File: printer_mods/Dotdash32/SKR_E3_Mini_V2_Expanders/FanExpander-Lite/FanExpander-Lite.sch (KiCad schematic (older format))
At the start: 31 parts, among them J1 FAN1_IN, J10 FAN2, J11 V_SELECT3, J12 V_SELECT4, J13 FAN3, J14 FAN4, J2 IO_PassThrough, J3 EXP1_IN, J6 V_SELECT1, J7 V_SELECT2, J9 FAN1, Q1 IRLML6344, Q2 IRLML6344, Q3 IRLML6344

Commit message: feat: init routing of Lite board
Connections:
- net FAN2: now also J3.8 (Pin_8); no longer J3.1 (Pin_1)
- net FAN3: now also J3.6 (Pin_6); no longer J3.3 (Pin_3)
- net FAN4: now also J3.2 (Pin_2); no longer J3.5 (Pin_5)
- net PASS0: now also J3.1 (Pin_1); no longer J3.7 (Pin_7)
- net PASS1: now also J3.3 (Pin_3); no longer J3.2 (Pin_2)
- net PASS2: now also J3.5 (Pin_5); no longer J3.6 (Pin_6)
- net PASS3: now also J3.7 (Pin_7); no longer J3.8 (Pin_8)
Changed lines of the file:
@@
 encoding utf-8
 Sheet 1 1
-Title "SKR E3 Mini Fan Expander"
-Date "2021-12-17"
-Rev "V0.1.0"
+Title "SKR E3 Mini Fan Expander Lite"
+Date "2021-12-18"
+Rev "V0.1.1"
 Comp "Voron Design"
 Comment1 "Drawn by Dotdash32 (JDeW)"
@@
 Wire Wire Line
 	550  1450 850  1450
-Text Label 550  1450 0    50   ~ 0
+Text Label 1650 1750 2    50   ~ 0
 FAN2
 Wire Wire Line
@@
 Wire Wire Line
 	850  1650 550  1650
-Text Label 550  1550 0    50   ~ 0
+Text Label 1650 1650 2    50   ~ 0
 FAN3
-Text Label 550  1650 0    50   ~ 0
+Text Label 1650 1450 2    50   ~ 0
 FAN4
 $Comp
@@
 Wire Wire Line
 	1350 1750 1650 1750
+Text Label 550  1450 0    50   ~ 0
+PASS0
+Text Label 550  1550 0    50   ~ 0
+PASS1
+Text Label 550  1650 0    50   ~ 0
+PASS2
 Text Label 550  1750 0    50   ~ 0
-PASS0
-Text Label 1650 1450 2    50   ~ 0
-PASS1
-Text Label 1650 1650 2    50   ~ 0
-PASS2
-Text Label 1650 1750 2    50   ~ 0
 PASS3
 Text Notes 2100 700  0    100  ~ 0

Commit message: chore: cleanup edges, silkscreen, making pretty
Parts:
- F1: value Polyfuse-2A -> Polyfuse-3A
- renumbered D3 to D1, D4 to D2, D5 to D3, D6 to D4, F3 to F2, J9 to J1, J10 to J2, J13 to J3, J14 to J4, J3 to J5, J1 to J6, J2 to J7, J6 to JP1, J7 to JP2, J11 to JP3, J12 to JP4, JP2 to JP5, R2 to R1, R3 to R2, R6 to R3, R5 to R4, R7 to R5, R11 to R6, R9 to R7, R12 to R9
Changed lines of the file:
@@
 $EndComp
 $Comp
-L Connector_Generic:Conn_01x02 J1
+L Connector_Generic:Conn_01x02 J6
 U 1 1 61C0DEDC
 P 800 3400
-F 0 "J1" H 718 3075 50  0000 C CNN
+F 0 "J6" H 718 3075 50  0000 C CNN
 F 1 "FAN1_IN" H 718 3166 50  0000 C CNN
 F 2 "Connectors_JST:JST_XH_B02B-XH-A_02x2.50mm_Straight" H 800 3400 50  0001 C CNN
@@
 P 2900 900
 F 0 "F1" V 3100 850 50  0000 L CNN
-F 1 "Polyfuse-2A" V 3000 650 50  0000 L CNN
+F 1 "Polyfuse-3A" V 3000 650 50  0000 L CNN
 F 2 "Fuse_Holders_and_Fuses:Fuse_SMD1206_HandSoldering" H 2950 700 50  0001 L CNN
 F 3 "~" H 2900 900 50  0001 C CNN
@@
 	500  3550 2000 3550
 $Comp
-L Connector_Generic:Conn_01x02 J9
+L Connector_Generic:Conn_01x02 J1
 U 1 1 61C7EF42
 P 7350 1400
-F 0 "J9" H 7430 1392 50  0000 L CNN
+F 0 "J1" H 7430 1392 50  0000 L CNN
 F 1 "FAN1" H 7430 1301 50  0000 L CNN
 F 2 "Connectors_JST:JST_XH_B02B-XH-A_02x2.50mm_Straight" H 7350 1400 50  0001 C CNN
@@
 $EndComp
 $Comp
-L Jumper:Jumper_3_Open J6
+L Jumper:Jumper_3_Open JP1
 U 1 1 61C814B1
 P 6800 1250
-F 0 "J6" H 6850 1450 50  0000 R CNN
+F 0 "JP1" H 6850 1450 50  0000 R CNN
 F 1 "V_SELECT1" H 7000 1350 50  0000 R CNN
 F 2 "Pin_Headers:Pin_Header_Straight_1x03_Pitch2.54mm" H 6800 1250 50  0001 C CNN
@@
 FAN1_Drive
 $Comp
-L Device:R_US R2
+L Device:R_US R1
 U 1 1 61C92F81
 P 6100 1500
-F 0 "R2" V 6305 1500 50  0000 C CNN
+F 0 "R1" V 6305 1500 50  0000 C CNN
 F 1 "560R" V 6214 1500 50  0000 C CNN
 F 2 "Resistors_SMD:R_0603_HandSoldering" V 6140 1490 50  0001 C CNN
@@
 $EndComp
 $Comp
-L Connector_Generic:Conn_01x02 J10
+L Connector_Generic:Conn_01x02 J2
 U 1 1 61CF5CB7
 P 9900 1400
-F 0 "J10" H 9980 1392 50  0000 L CNN
+F 0 "J2" H 9980 1392 50  0000 L CNN
 F 1 "FAN2" H 9980 1301 50  0000 L CNN
 F 2 "Connectors_JST:JST_XH_B02B-XH-A_02x2.50mm_Straight" H 9900 1400 50  0001 C CNN
@@
 $EndComp
 $Comp
-L Jumper:Jumper_3_Open J7
+L Jumper:Jumper_3_Open JP2
 U 1 1 61CF5CBD
 P 9350 1250
-F 0 "J7" H 9400 1450 50  0000 R CNN
+F 0 "JP2" H 9400 1450 50  0000 R CNN
 F 1 "V_SELECT2" H 9550 1350 50  0000 R CNN
 F 2 "Pin_Headers:Pin_Header_Straight_1x03_Pitch2.54mm" H 9350 1250 50  0001 C CNN
@@
 $EndComp
 $Comp
-L Device:R_US R3
+L Device:R_US R2
 U 1 1 61CF5CD5
 P 8700 1450
-F 0 "R3" V 8905 1450 50  0000 C CNN
+F 0 "R2" V 8905 1450 50  0000 C CNN
 F 1 "560R" V 8814 1450 50  0000 C CNN
 F 2 "Resistors_SMD:R_0603_HandSoldering" V 8740 1440 50  0001 C CNN
@@
 $EndComp
 $Comp
-L Device:LED D4
+L Device:LED D2
 U 1 1 61CF5CDB
 P 8900 1600
-F 0 "D4" V 8939 1483 50  0000 R CNN
+F 0 "D2" V 8939 1483 50  0000 R CNN
 F 1 "LED" V 8848 1483 50  0000 R CNN
 F 2 "LEDs:LED_0603_HandSoldering" H 8900 1600 50  0001 C CNN
@@
 Connection ~ 9550 1600
 $Comp
-L Device:R_US R6
+L Device:R_US R3
 U 1 1 61D23E6E
 P 9000 1950
-F 0 "R6" V 8795 1950 50  0000 C CNN
+F 0 "R3" V 8795 1950 50  0000 C CNN
 F 1 "100R" V 8886 1950 50  0000 C CNN
 F 2 "Resistors_SMD:R_0603_HandSoldering" V 9040 1940 50  0001 C CNN
@@
 	9550 1600 9550 1750
 $Comp
-L Device:LED D3
+L Device:LED D1
 U 1 1 61C95144
 P 6350 1650
-F 0 "D3" V 6389 1533 50  0000 R CNN
+F 0 "D1" V 6389 1533 50  0000 R CNN
 F 1 "LED" V 6298 1533 50  0000 R CNN
 F 2 "LEDs:LED_0603_HandSoldering" H 6350 1650 50  0001 C CNN
@@
 $EndComp
 $Comp
-L Connector_Generic:Conn_01x02 J13
+L Connector_Generic:Conn_01x02 J3
 U 1 1 61DAD553
 P 7450 3100
-F 0 "J13" H 7530 3092 50  0000 L CNN
+F 0 "J3" H 7530 3092 50  0000 L CNN
 F 1 "FAN3" H 7530 3001 50  0000 L CNN
 F 2 "Connectors_JST:JST_XH_B02B-XH-A_02x2.50mm_Straight" H 7450 3100 50  0001 C CNN
@@
 $EndComp
 $Comp
-L Jumper:Jumper_3_Open J11
+L Jumper:Jumper_3_Open JP3
 U 1 1 61DAD559
 P 6900 2950
-F 0 "J11" H 6950 3150 50  0000 R CNN
+F 0 "JP3" H 6950 3150 50  0000 R CNN
 F 1 "V_SELECT3" H 7100 3050 50  0000 R CNN
 F 2 "Pin_Headers:Pin_Header_Straight_1x03_Pitch2.54mm" H 6900 2950 50  0001 C CNN
@@
 $EndComp
 $Comp
-L Device:LED D5
+L Device:LED D3
 U 1 1 61DAD575
 P 6450 3300
-F 0 "D5" V 6489 3183 50  0000 R CNN
+F 0 "D3" V 6489 3183 50  0000 R CNN
 F 1 "LED" V 6398 3183 50  0000 R CNN
 F 2 "LEDs:LED_0603_HandSoldering" H 6450 3300 50  0001 C CNN
@@
 Connection ~ 7100 3300
 $Comp
-L Device:R_US R11
+L Device:R_US R6
 U 1 1 61DAD584
 P 6550 3650
-F 0 "R11" V 6345 3650 50  0000 C CNN
+F 0 "R6" V 6345 3650 50  0000 C CNN
 F 1 "100R" V 6436 3650 50  0000 C CNN
 F 2 "Resistors_SMD:R_0603_HandSoldering" V 6590 3640 50  0001 C CNN
@@
 $EndComp
 $Comp
-L Device:R_US R9
+L Device:R_US R7
 U 1 1 61DAD58A
 P 6550 3950
-F 0 "R9" V 6345 3950 50  0000 C CNN
+F 0 "R7" V 6345 3950 50  0000 C CNN
 F 1 "100k" V 6436 3950 50  0000 C CNN
 F 2 "Resistors_SMD:R_0603_HandSoldering" V 6590 3940 50  0001 C CNN
@@
 $EndComp
 $Comp
-L Connector_Generic:Conn_01x02 J14
+L Connector_Generic:Conn_01x02 J4
 U 1 1 61DF6C6B
 P 9950 3100
-F 0 "J14" H 10030 3092 50  0000 L CNN
+F 0 "J4" H 10030 3092 50  0000 L CNN
 F 1 "FAN4" H 10030 3001 50  0000 L CNN
 F 2 "Connectors_JST:JST_XH_B02B-XH-A_02x2.50mm_Straight" H 9950 3100 50  0001 C CNN
@@
 $EndComp
 $Comp
-L Jumper:Jumper_3_Open J12
+L Jumper:Jumper_3_Open JP4
 U 1 1 61DF6C71
 P 9400 2950
-F 0 "J12" H 9450 3150 50  0000 R CNN
+F 0 "JP4" H 9450 3150 50  0000 R CNN
 F 1 "V_SELECT4" H 9600 3050 50  0000 R CNN
 F 2 "Pin_Headers:Pin_Header_Straight_1x03_Pitch2.54mm" H 9400 2950 50  0001 C CNN
@@
 $EndComp
 $Comp
-L Device:LED D6
+L Device:LED D4
 U 1 1 61DF6C8D
 P 8950 3300
-F 0 "D6" V 8989 3183 50  0000 R CNN
+F 0 "D4" V 8989 3183 50  0000 R CNN
 F 1 "LED" V 8898 3183 50  0000 R CNN
 F 2 "LEDs:LED_0603_HandSoldering" H 8950 3300 50  0001 C CNN
@@
 Connection ~ 9600 3300
 $Comp
-L Device:R_US R12
+L Device:R_US R9
 U 1 1 61DF6C9C
 P 9050 3650
-F 0 "R12" V 8845 3650 50  0000 C CNN
+F 0 "R9" V 8845 3650 50  0000 C CNN
 F 1 "100R" V 8936 3650 50  0000 C CNN
 F 2 "Resistors_SMD:R_0603_HandSoldering" V 9090 3640 50  0001 C CNN
@@
 	650  1850 850  1850
 $Comp
-L Device:Polyfuse F3
+L Device:Polyfuse F2
 U 1 1 61C255C6
 P 2900 1250
-F 0 "F3" V 2700 1200 50  0000 L CNN
+F 0 "F2" V 2700 1200 50  0000 L CNN
 F 1 "Polyfuse-1A" V 2800 1000 50  0000 L CNN
 F 2 "Fuse_Holders_and_Fuses:Fuse_SMD1206_HandSoldering" H 2950 1050 50  0001 L CNN
@@
 SKR Mini E3 V2 EXP1\nPB5       | PA15\nTX1/PA9  | RST\nRX1/PA10 | PB9\nPB8       | PB15\nGND       | +5V
 $Comp
-L Connector_Generic:Conn_02x05_Odd_Even J3
+L Connector_Generic:Conn_02x05_Odd_Even J5
 U 1 1 61BFB492
 P 1050 1650
-F 0 "J3" H 1100 2067 50  0000 C CNN
+F 0 "J5" H 1100 2067 50  0000 C CNN
 F 1 "EXP1_IN" H 1100 1976 50  0000 C CNN
 F 2 "Connectors_Multicomp:Multicomp_MC9A12-1034_2x05x2.54mm_Straight" H 1050 1650 50  0001 C CNN
@@
 $EndComp
 $Comp
-L Jumper:SolderJumper_2_Bridged JP2
+L Jumper:SolderJumper_2_Bridged JP5
 U 1 1 6239146B
 P 2600 2000
-F 0 "JP2" H 2600 2205 50  0000 C CNN
+F 0 "JP5" H 2600 2205 50  0000 C CNN
 F 1 "LED_ENABLE" H 2600 2114 50  0000 C CNN
 F 2 "Jumper:SolderJumper-2_P1.3mm_Bridged_RoundedPad1.0x1.5mm" H 2600 2000 50  0001 C CNN
@@
 	8450 1950 8800 1950
 $Comp
-L Device:R_US R5
+L Device:R_US R4
 U 1 1 61D251AF
 P 9000 2250
-F 0 "R5" V 9200 2200 50  0000 L CNN
+F 0 "R4" V 9200 2200 50  0000 L CNN
 F 1 "100k" V 9100 2150 50  0000 L CNN
 F 2 "Resistors_SMD:R_0603_HandSoldering" V 9040 2240 50  0001 C CNN
@@
 	6300 3300 6250 3300
 $Comp
-L Device:R_US R7
+L Device:R_US R5
 U 1 1 61DAD56F
 P 6250 3150
-F 0 "R7" V 6455 3150 50  0000 C CNN
+F 0 "R5" V 6455 3150 50  0000 C CNN
 F 1 "560R" V 6364 3150 50  0000 C CNN
 F 2 "Resistors_SMD:R_0603_HandSoldering" V 6290 3140 50  0001 C CNN
@@
 	3500 500  3500 2450
 $Comp
-L Connector_Generic:Conn_02x04_Odd_Even J2
+L Connector_Generic:Conn_02x04_Odd_Even J7
 U 1 1 62877243
 P 4350 1100
-F 0 "J2" H 4400 1417 50  0000 C CNN
+F 0 "J7" H 4400 1417 50  0000 C CNN
 F 1 "IO_PassThrough" H 4400 1326 50  0000 C CNN
 F 2 "Pin_Headers:Pin_Header_Straight_2x04_Pitch2.54mm" H 4350 1100 50  0001 C CNN

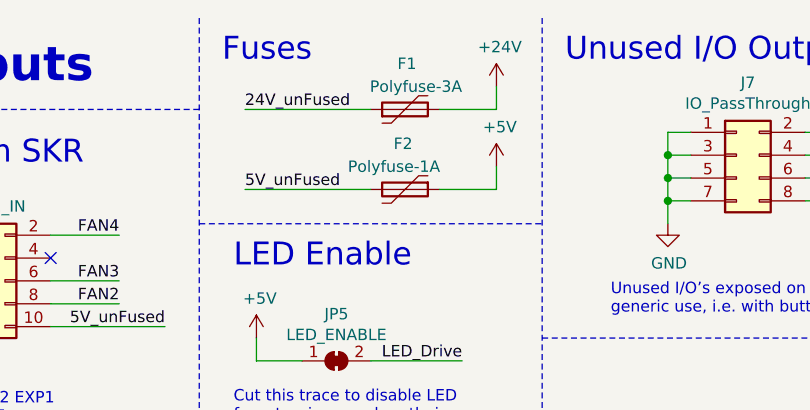
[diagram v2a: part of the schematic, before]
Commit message: feat: redo layout to use backside SMD parts
move to align with main board version, compactness!
Also moving to larger THT PTC fuses
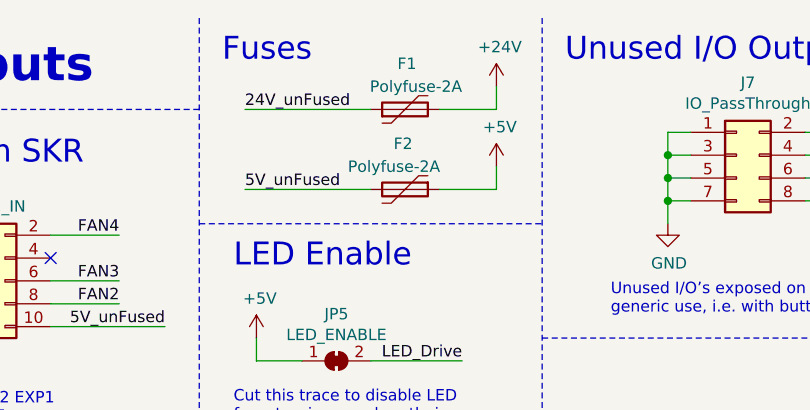
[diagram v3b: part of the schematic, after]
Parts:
- D1, D2, D3, D4: footprint LEDs:LED_0603_HandSoldering -> LED_SMD:LED_1206_3216Metric_ReverseMount_Hole1.8x2.4mm
- F1: value Polyfuse-3A -> Polyfuse-2A; footprint Fuse_Holders_and_Fuses:Fuse_SMD1206_HandSoldering -> Fuse:Fuse_Bourns_MF-RHT200
- F2: value Polyfuse-1A -> Polyfuse-2A; footprint Fuse_Holders_and_Fuses:Fuse_SMD1206_HandSoldering -> Fuse:Fuse_Bourns_MF-RHT200
- R1, R10, R2, R3, R4, R5, R6, R7, R8, R9: footprint Resistors_SMD:R_0603_HandSoldering -> Resistors_SMD:R_0603
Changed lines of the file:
@@
 P 2900 900
 F 0 "F1" V 3100 850 50  0000 L CNN
-F 1 "Polyfuse-3A" V 3000 650 50  0000 L CNN
-F 2 "Fuse_Holders_and_Fuses:Fuse_SMD1206_HandSoldering" H 2950 700 50  0001 L CNN
+F 1 "Polyfuse-2A" V 3000 650 50  0000 L CNN
+F 2 "Fuse:Fuse_Bourns_MF-RHT200" H 2950 700 50  0001 L CNN
 F 3 "~" H 2900 900 50  0001 C CNN
 	1    2900 900
@@
 F 0 "R1" V 6305 1500 50  0000 C CNN
 F 1 "560R" V 6214 1500 50  0000 C CNN
-F 2 "Resistors_SMD:R_0603_HandSoldering" V 6140 1490 50  0001 C CNN
+F 2 "Resistors_SMD:R_0603" V 6140 1490 50  0001 C CNN
 F 3 "~" H 6100 1500 50  0001 C CNN
 	1    6100 1500
@@
 F 0 "R2" V 8905 1450 50  0000 C CNN
 F 1 "560R" V 8814 1450 50  0000 C CNN
-F 2 "Resistors_SMD:R_0603_HandSoldering" V 8740 1440 50  0001 C CNN
+F 2 "Resistors_SMD:R_0603" V 8740 1440 50  0001 C CNN
 F 3 "~" H 8700 1450 50  0001 C CNN
 	1    8700 1450
@@
 F 0 "D2" V 8939 1483 50  0000 R CNN
 F 1 "LED" V 8848 1483 50  0000 R CNN
-F 2 "LEDs:LED_0603_HandSoldering" H 8900 1600 50  0001 C CNN
+F 2 "LED_SMD:LED_1206_3216Metric_ReverseMount_Hole1.8x2.4mm" H 8900 1600 50  0001 C CNN
 F 3 "~" H 8900 1600 50  0001 C CNN
 	1    8900 1600
@@
 F 0 "R3" V 8795 1950 50  0000 C CNN
 F 1 "100R" V 8886 1950 50  0000 C CNN
-F 2 "Resistors_SMD:R_0603_HandSoldering" V 9040 1940 50  0001 C CNN
+F 2 "Resistors_SMD:R_0603" V 9040 1940 50  0001 C CNN
 F 3 "~" H 9000 1950 50  0001 C CNN
 	1    9000 1950
@@
 F 0 "D1" V 6389 1533 50  0000 R CNN
 F 1 "LED" V 6298 1533 50  0000 R CNN
-F 2 "LEDs:LED_0603_HandSoldering" H 6350 1650 50  0001 C CNN
+F 2 "LED_SMD:LED_1206_3216Metric_ReverseMount_Hole1.8x2.4mm" H 6350 1650 50  0001 C CNN
 F 3 "~" H 6350 1650 50  0001 C CNN
 	1    6350 1650
@@
 F 0 "D3" V 6489 3183 50  0000 R CNN
 F 1 "LED" V 6398 3183 50  0000 R CNN
-F 2 "LEDs:LED_0603_HandSoldering" H 6450 3300 50  0001 C CNN
+F 2 "LED_SMD:LED_1206_3216Metric_ReverseMount_Hole1.8x2.4mm" H 6450 3300 50  0001 C CNN
 F 3 "~" H 6450 3300 50  0001 C CNN
 	1    6450 3300
@@
 F 0 "R6" V 6345 3650 50  0000 C CNN
 F 1 "100R" V 6436 3650 50  0000 C CNN
-F 2 "Resistors_SMD:R_0603_HandSoldering" V 6590 3640 50  0001 C CNN
+F 2 "Resistors_SMD:R_0603" V 6590 3640 50  0001 C CNN
 F 3 "~" H 6550 3650 50  0001 C CNN
 	1    6550 3650
@@
 F 0 "R7" V 6345 3950 50  0000 C CNN
 F 1 "100k" V 6436 3950 50  0000 C CNN
-F 2 "Resistors_SMD:R_0603_HandSoldering" V 6590 3940 50  0001 C CNN
+F 2 "Resistors_SMD:R_0603" V 6590 3940 50  0001 C CNN
 F 3 "~" H 6550 3950 50  0001 C CNN
 	1    6550 3950
@@
 F 0 "R8" V 8955 3150 50  0000 C CNN
 F 1 "560R" V 8864 3150 50  0000 C CNN
-F 2 "Resistors_SMD:R_0603_HandSoldering" V 8790 3140 50  0001 C CNN
+F 2 "Resistors_SMD:R_0603" V 8790 3140 50  0001 C CNN
 F 3 "~" H 8750 3150 50  0001 C CNN
 	1    8750 3150
@@
 F 0 "D4" V 8989 3183 50  0000 R CNN
 F 1 "LED" V 8898 3183 50  0000 R CNN
-F 2 "LEDs:LED_0603_HandSoldering" H 8950 3300 50  0001 C CNN
+F 2 "LED_SMD:LED_1206_3216Metric_ReverseMount_Hole1.8x2.4mm" H 8950 3300 50  0001 C CNN
 F 3 "~" H 8950 3300 50  0001 C CNN
 	1    8950 3300
@@
 F 0 "R9" V 8845 3650 50  0000 C CNN
 F 1 "100R" V 8936 3650 50  0000 C CNN
-F 2 "Resistors_SMD:R_0603_HandSoldering" V 9090 3640 50  0001 C CNN
+F 2 "Resistors_SMD:R_0603" V 9090 3640 50  0001 C CNN
 F 3 "~" H 9050 3650 50  0001 C CNN
 	1    9050 3650
@@
 F 0 "R10" V 8845 3950 50  0000 C CNN
 F 1 "100k" V 8936 3950 50  0000 C CNN
-F 2 "Resistors_SMD:R_0603_HandSoldering" V 9090 3940 50  0001 C CNN
+F 2 "Resistors_SMD:R_0603" V 9090 3940 50  0001 C CNN
 F 3 "~" H 9050 3950 50  0001 C CNN
 	1    9050 3950
@@
 P 2900 1250
 F 0 "F2" V 2700 1200 50  0000 L CNN
-F 1 "Polyfuse-1A" V 2800 1000 50  0000 L CNN
-F 2 "Fuse_Holders_and_Fuses:Fuse_SMD1206_HandSoldering" H 2950 1050 50  0001 L CNN
+F 1 "Polyfuse-2A" V 2800 1000 50  0000 L CNN
+F 2 "Fuse:Fuse_Bourns_MF-RHT200" H 2950 1050 50  0001 L CNN
 F 3 "~" H 2900 1250 50  0001 C CNN
 	1    2900 1250
@@
 F 0 "R4" V 9200 2200 50  0000 L CNN
 F 1 "100k" V 9100 2150 50  0000 L CNN
-F 2 "Resistors_SMD:R_0603_HandSoldering" V 9040 2240 50  0001 C CNN
+F 2 "Resistors_SMD:R_0603" V 9040 2240 50  0001 C CNN
 F 3 "~" H 9000 2250 50  0001 C CNN
 	1    9000 2250
@@
 F 0 "R5" V 6455 3150 50  0000 C CNN
 F 1 "560R" V 6364 3150 50  0000 C CNN
-F 2 "Resistors_SMD:R_0603_HandSoldering" V 6290 3140 50  0001 C CNN
+F 2 "Resistors_SMD:R_0603" V 6290 3140 50  0001 C CNN
 F 3 "~" H 6250 3150 50  0001 C CNN
 	1    6250 3150

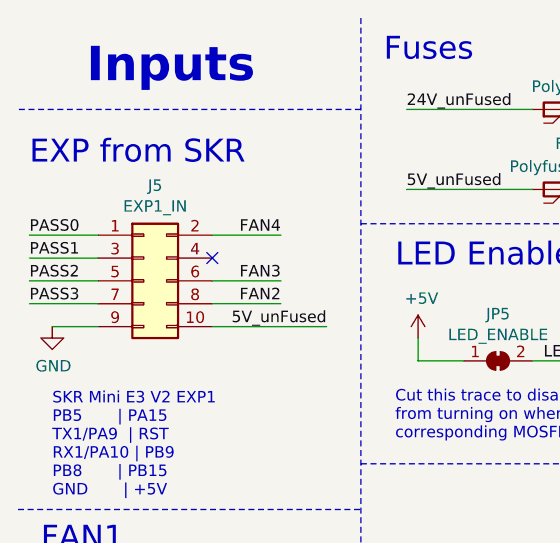
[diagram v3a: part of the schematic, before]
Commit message: feat: routing the board
no external 5V tap, but it'll probably be fine??
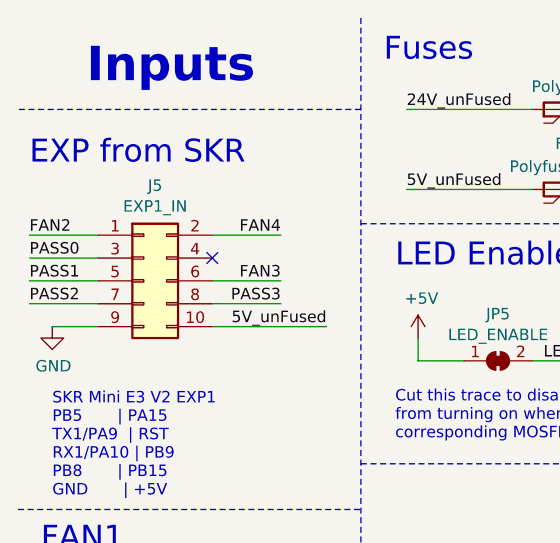
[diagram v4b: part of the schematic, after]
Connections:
- net FAN2: now also J5.1 (Pin_1); no longer J5.8 (Pin_8)
- net PASS0: now also J5.3 (Pin_3); no longer J5.1 (Pin_1)
- net PASS1: now also J5.5 (Pin_5); no longer J5.3 (Pin_3)
- net PASS2: now also J5.7 (Pin_7); no longer J5.5 (Pin_5)
- net PASS3: now also J5.8 (Pin_8); no longer J5.7 (Pin_7)
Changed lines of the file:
@@
 Wire Wire Line
 	550  1450 850  1450
-Text Label 1650 1750 2    50   ~ 0
+Text Label 550  1450 0    50   ~ 0
 FAN2
 Wire Wire Line
@@
 Wire Wire Line
 	1350 1750 1650 1750
-Text Label 550  1450 0    50   ~ 0
+Text Label 550  1550 0    50   ~ 0
 PASS0
-Text Label 550  1550 0    50   ~ 0
+Text Label 550  1650 0    50   ~ 0
 PASS1
-Text Label 550  1650 0    50   ~ 0
+Text Label 550  1750 0    50   ~ 0
 PASS2
-Text Label 550  1750 0    50   ~ 0
+Text Label 1650 1750 2    50   ~ 0
 PASS3
 Text Notes 2100 700  0    100  ~ 0
